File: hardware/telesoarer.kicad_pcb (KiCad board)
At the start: 2 copper layers, 37.2 x 16 mm, 30 parts, among them IC1 ATMEGA328P, K1 RC SIG IN, K2 G T R, P1 ATMEL ISP, P2 PZ, P3 PZ_IN, P4 AOUT, Q1 BC847C, Q2 2N7000, U1 MS5611

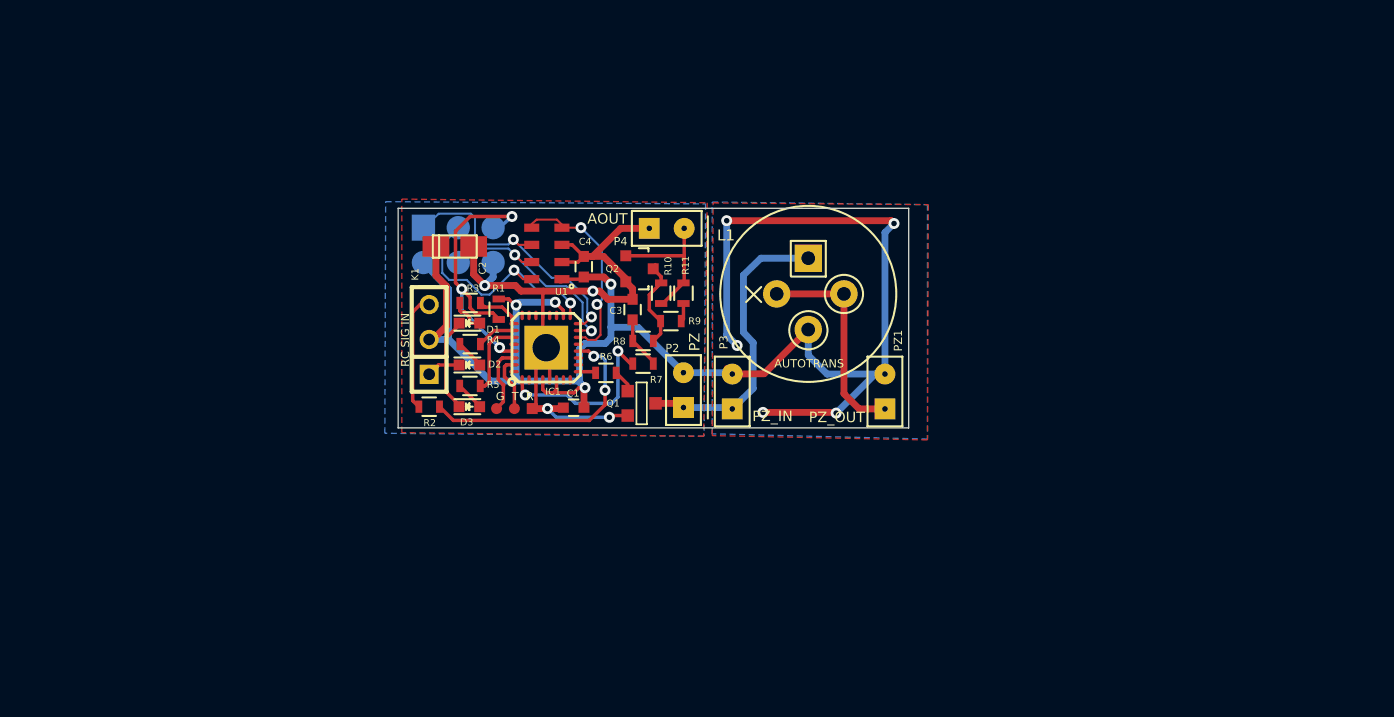
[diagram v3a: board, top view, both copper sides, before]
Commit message: Switching to NXP ARM chip. Added reference files.
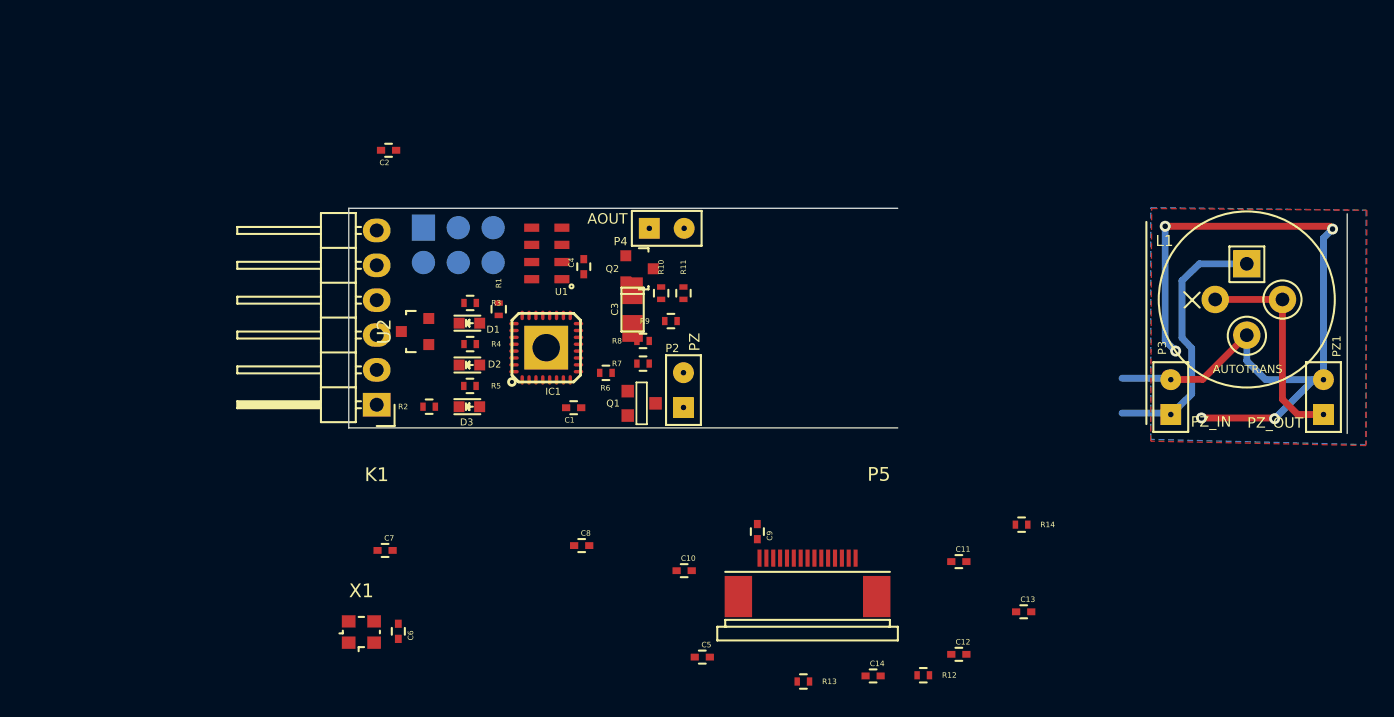
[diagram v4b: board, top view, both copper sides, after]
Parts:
- removed K2: G T R, footprints:TP-3
- added C10: 1u, footprints:C_0402, F.Cu at (64.4, 57.4)
- added C11: 1u, footprints:C_0402, F.Cu at (84.5, 56.7)
- added C12: 1u, footprints:C_0402, F.Cu at (84.5, 63.5)
- added C13: 2u2, footprints:C_0402, F.Cu at (89.2, 60.4)
- added C14: 2u2, footprints:C_0402, F.Cu at (78.2, 65.1)
- added C5: 0u1, footprints:C_0402, F.Cu at (65.8, 63.7)
- added C6: 18p, footprints:C_0402, F.Cu at (43.6, 61.8)
- added C7: 0u1, footprints:C_0402, F.Cu at (42.6, 55.9)
- added C8: 0u1, footprints:C_0402, F.Cu at (57.0, 55.6)
- added C9: 1u, footprints:C_0402, F.Cu at (69.8, 54.6)
- added P5: OLED 0.91" 128x32, footprints:ZIF_FPC15, F.Cu at (73.4, 56.5)
- added R12: 330K, footprints:R_0402, F.Cu at (81.9, 65.0)
- added R13: 1K, footprints:R_0402, F.Cu at (73.1, 65.5)
- added R14: 390K, footprints:R_0402, F.Cu at (89.0, 54.1)
- added U2: MCP1703T-3302, footprints:SOT-23A, F.Cu at (44.8, 40.0)
- added X1: 16MHz, Crystals:Crystal_SMD_2520_4Pads, F.Cu at (40.9, 61.9)
- C1: footprint footprints:C_0603 -> footprints:C_0402
- C2: value 22u -> 0u1; footprint footprints:TantalC_SizeS_EIA-3216 -> footprints:C_0402
- C3: value 0u1 -> 22u; footprint footprints:C_0603 -> footprints:TantalC_SizeS_EIA-3216
- C4: value 0u1 -> 18p; footprint footprints:C_0603 -> footprints:C_0402
- K1: value RC SIG IN -> DATA; footprint footprints:SIL-3 -> Pin_Headers:Pin_Header_Angled_1x06
- R1: value 5K6 -> 10K; footprint footprints:R_0603 -> footprints:R_0402
- R10: value 330K -> 220K; footprint footprints:R_0603 -> footprints:R_0402
- R11: value 1K -> 220K; footprint footprints:R_0603 -> footprints:R_0402
- R2: value 200 -> 1K; footprint footprints:R_0603 -> footprints:R_0402
- R3, R4, R5, R6: footprint footprints:R_0603 -> footprints:R_0402
- R7: value 56K -> 0; footprint footprints:R_0603 -> footprints:R_0402
- R8: value 220K -> 56K; footprint footprints:R_0603 -> footprints:R_0402
- R9: value 220K -> 1K; footprint footprints:R_0603 -> footprints:R_0402
- moved P3 32.0 mm to (99.9, 44.8)
- moved L1 32.0 mm to (105.4, 37.6)
- moved PZ1 32.0 mm to (111.0, 44.8)
- moved C2 8.51 mm to (42.9, 26.8)
- moved K1 6.10 mm to (42.0, 45.3), turned to 180 degrees
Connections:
- net /~SS renamed /SENS_~SS
- C1 pad 1: +5V -> +3V3
- C1 pad 2: GND -> (no net)
- C2 pad 1: +5V -> /~RESET
- C2 pad 2: GND -> Net-(C2-Pad2)
- C3 pad 1: Net-(C3-Pad1) -> +BATT
- C4 pad 1: +5V -> Net-(C4-Pad1)
- IC1 pad 10: Net-(IC1-Pad10) -> /~RES
- IC1 pad 11: Net-(IC1-Pad11) -> /D/~C
- IC1 pad 13: Net-(IC1-Pad13) -> /OLED_~SS
- IC1 pad 18: +5V -> +3V3
- IC1 pad 19: Net-(IC1-Pad19) -> (no net)
- IC1 pad 2: Net-(IC1-Pad2) -> (no net)
- IC1 pad 20: Net-(IC1-Pad20) -> (no net)
- IC1 pad 22: Net-(IC1-Pad22) -> (no net)
- IC1 pad 23: Net-(IC1-Pad23) -> (no net)
- IC1 pad 24: Net-(IC1-Pad24) -> (no net)
- IC1 pad 28: Net-(IC1-Pad28) -> (no net)
- IC1 pad 29: /RESET -> /~RESET
- IC1 pad 4: +5V -> +3V3
- IC1 pad 6: +5V -> +3V3
- IC1 pad 7: Net-(IC1-Pad7) -> Net-(C4-Pad1)
- K1 pad 2: +5V -> +BATT
- L1 pad 2: +5V -> +BATT
- P1 pad 2: +5V -> +3V3
- P1 pad 5: /RESET -> /~RESET
- P2 pad 2: +5V -> +BATT
- P3 pad 2: +5V -> +BATT
- PZ1 pad 2: +5V -> +BATT
- R1 pad 1: /RESET -> /~RESET
- R1 pad 2: +5V -> +3V3
- R10 pad 1: Net-(P4-Pad2) -> Net-(Q2-Pad3)
- R10 pad 2: Net-(Q2-Pad3) -> Net-(C8-Pad1)
- R11 pad 2: Net-(P4-Pad2) -> Net-(Q2-Pad3)
- R6 pad 1: Net-(Q1-Pad1) -> /RX
- R6 pad 2: Net-(IC1-Pad9) -> Net-(IC1-Pad30)
- R7 pad 1: Net-(C3-Pad1) -> /TX
- R7 pad 2: Net-(IC1-Pad1) -> Net-(IC1-Pad31)
- R8 pad 1: Net-(Q2-Pad3) -> Net-(C8-Pad1)
- R8 pad 2: Net-(C3-Pad1) -> Net-(IC1-Pad1)
- R9 pad 1: +3V3 -> Net-(Q1-Pad1)
- R9 pad 2: Net-(Q2-Pad3) -> Net-(IC1-Pad9)
- U1 pad 1: +5V -> +3V3
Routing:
- net +5V: track 126.1 -> 0.00 mm, vias 9 -> 0
- net GND: track 61.8 -> 0.00 mm, vias 4 -> 0
- net +BATT: track 0.00 -> 61.6 mm, vias 0 -> 5
- net /RESET: track 21.3 -> 0.00 mm, vias 3 -> 0
- net /MISO: track 20.5 -> 0.00 mm, vias 2 -> 0
- net Net-(IC1-Pad12): track 18.3 -> 0.00 mm, vias 2 -> 0
- net /SCK: track 17.8 -> 0.00 mm, vias 2 -> 0
- net /MOSI: track 16.2 -> 0.00 mm, vias 2 -> 0
- net /SENS_~SS: track 14.7 -> 0.00 mm, vias 2 -> 0
- net Net-(IC1-Pad1): track 13.0 -> 0.00 mm, vias 2 -> 0
- net Net-(P4-Pad2): track 10.6 -> 0.00 mm
- net /SIG: track 8.51 -> 0.00 mm
- net Net-(Q2-Pad3): track 6.68 -> 0.00 mm
- net /LED_GREEN: track 5.38 -> 0.00 mm
- net Net-(IC1-Pad30): track 5.12 -> 0.00 mm
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- added copper zone on B.Cu, net +BATT
- added copper zone on F.Cu, net +BATT
- removed copper zone on B.Cu, net +5V
- removed copper zone on F.Cu, net +5V
- removed copper zone on B.Cu, net GND
- removed copper zone on F.Cu, net GND
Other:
- board size 37.2 x 16 mm -> 72.8 x 16.4 mm

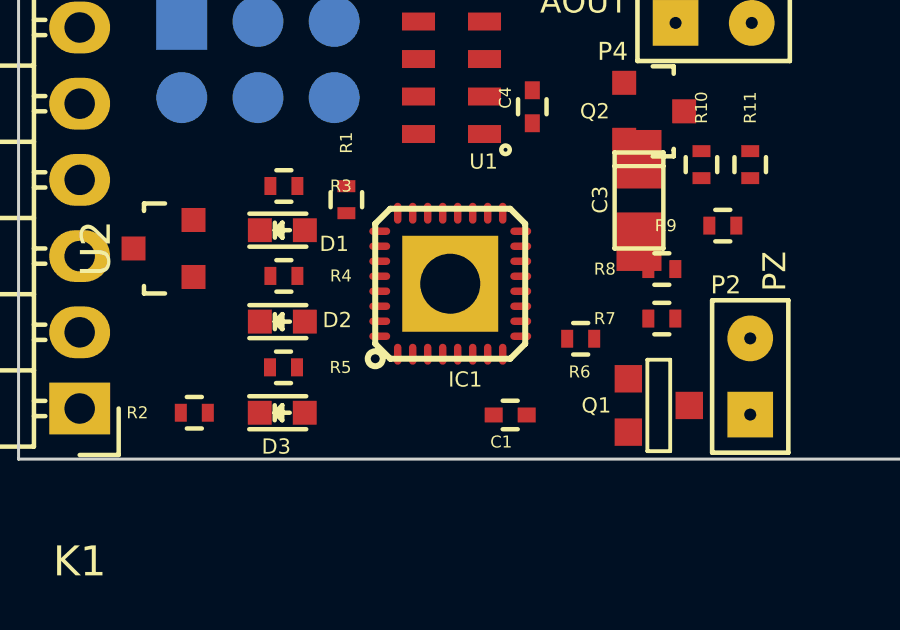
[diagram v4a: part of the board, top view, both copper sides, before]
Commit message: Ripping things apart for the change to STM32 chipa
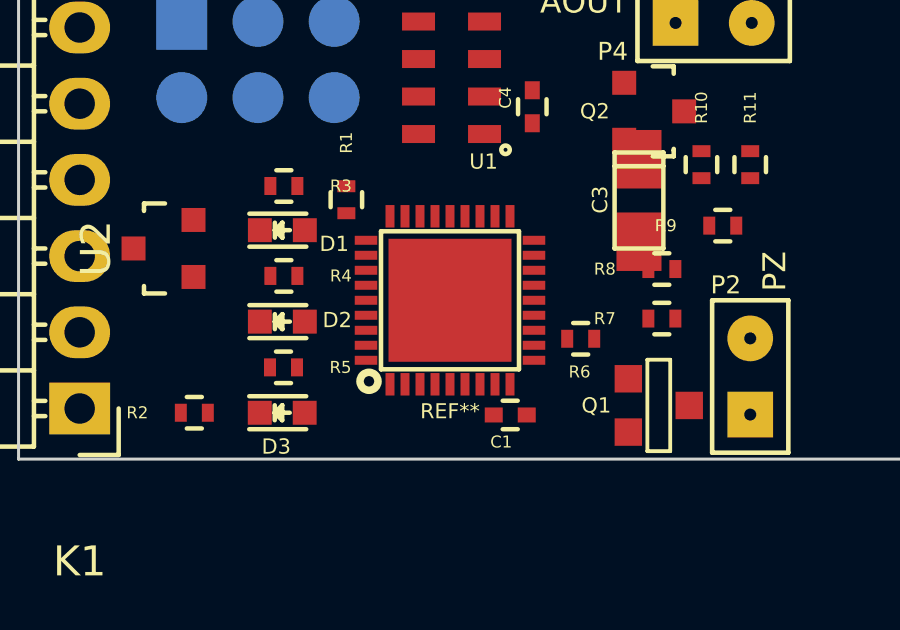
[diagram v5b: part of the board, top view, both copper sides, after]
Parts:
- removed IC1: ATMEGA328P, footprints:MLF-32_2mmVIA_SINK
- added REF**: VFQFPN36_0.5_6x6, footprints:VFQFPN36_0.5_6x6, F.Cu at (54.4, 41.7)

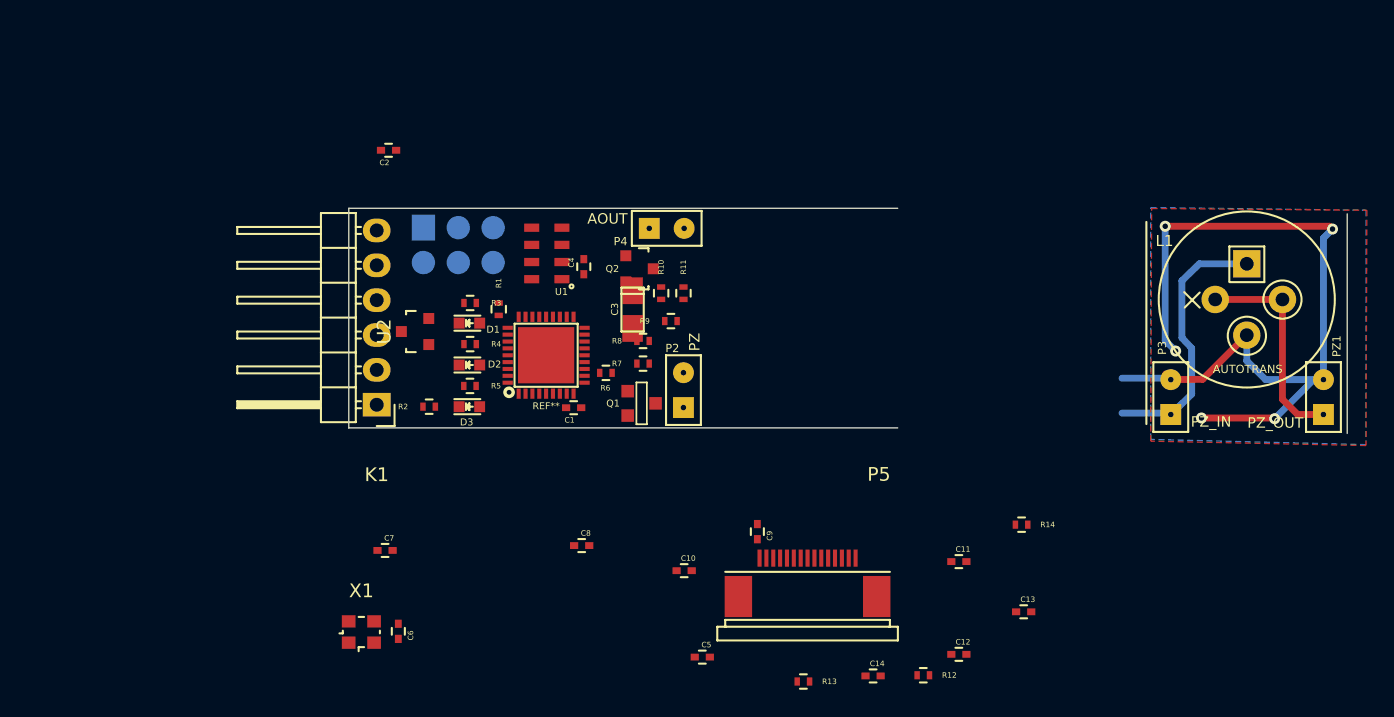
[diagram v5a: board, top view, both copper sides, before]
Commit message: Work on STM32 / OLED PCB design begins
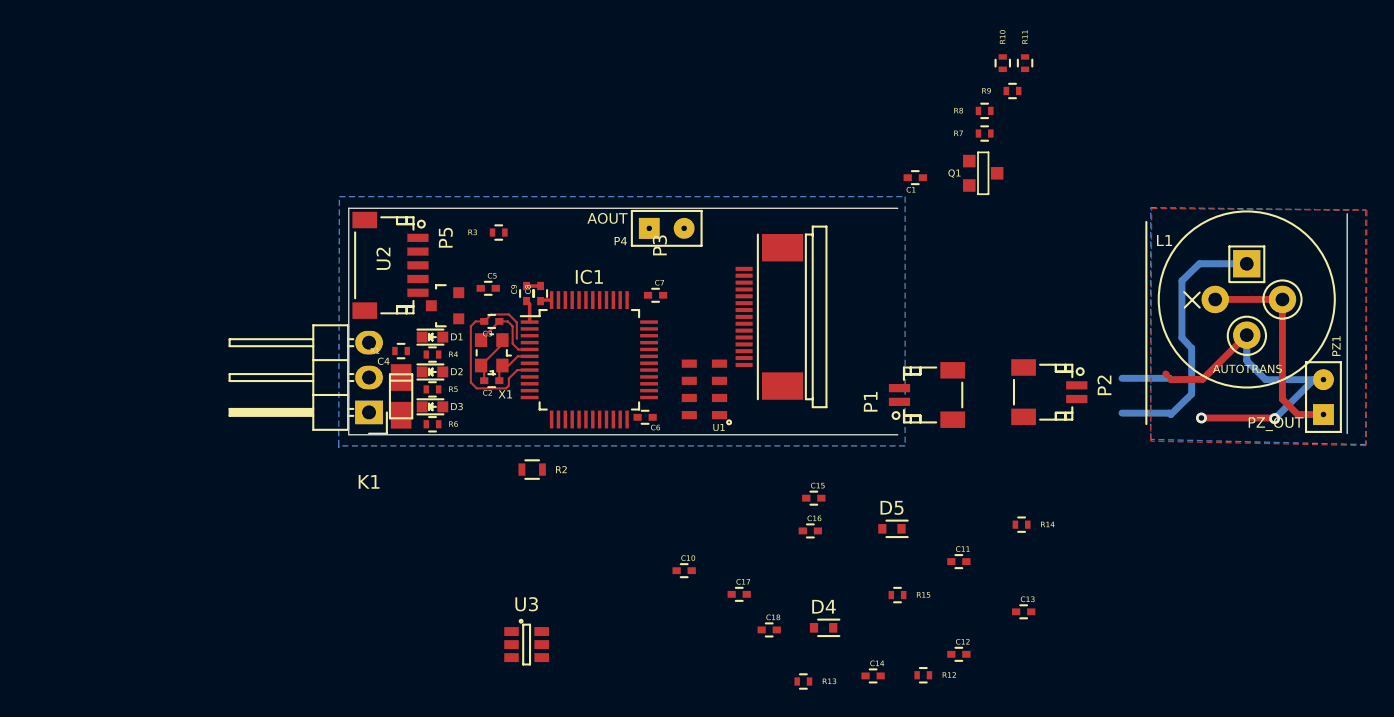
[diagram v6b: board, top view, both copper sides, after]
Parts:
- removed Q2: 2N7000, TO_SOT_Packages_SMD:SOT-23
- removed REF**: VFQFPN36_0.5_6x6, footprints:VFQFPN36_0.5_6x6
- added C15: 1u, footprints:C_0402, F.Cu at (73.9, 52.1)
- added C16: 1u, footprints:C_0402, F.Cu at (73.6, 54.5)
- added C17: 2u2, footprints:C_0402, F.Cu at (68.5, 59.1)
- added C18: 2u2, footprints:C_0402, F.Cu at (70.6, 61.7)
- added D4: D_Schottky, Diodes_SMD:SOD-523, F.Cu at (74.6, 61.6)
- added D5: D_Schottky, Diodes_SMD:SOD-523, F.Cu at (79.6, 54.4)
- added IC1: STM32F103CBT6, footprints:LQFP-48_7x7mm_Pitch0.5mm, F.Cu at (57.5, 42.0)
- added R15: 100K, footprints:R_0402, F.Cu at (80.0, 59.2)
- added U3: AD8027ARTZ, TO_SOT_Packages_SMD:SOT-23-6, F.Cu at (53.0, 62.8)
- C10, C11, C9: value 1u -> 0u1
- C13: value 2u2 -> 1u
- C14: value 2u2 -> 0u1
- C2: value 0u1 -> 18p
- C3: value 22u -> 18p; footprint footprints:TantalC_SizeS_EIA-3216 -> footprints:C_0402
- C4: value 18p -> 22u; footprint footprints:C_0402 -> footprints:TantalC_SizeS_EIA-3216
- C6: value 18p -> 0u1
- K1: value DATA -> RC_SIG; footprint Pin_Headers:Pin_Header_Angled_1x06 -> Pin_Headers:Pin_Header_Angled_1x03
- P1: value ATMEL ISP -> PZ; footprint POGO_ISP_3x2 -> Connectors_JST:JST_SH_SM02B-SRSS-TB_02x1.00mm_Angled; moved to F.Cu
- P2: value PZ -> PZ_IN; footprint footprints:PIN_ARRAY_2X1 -> Connectors_JST:JST_SH_SM02B-SRSS-TB_02x1.00mm_Angled
- P3: value PZ_IN -> OLED 0.91" 128x32; footprint footprints:PIN_ARRAY_2X1 -> footprints:ZIF_FPC15
- P5: value OLED 0.91" 128x32 -> CONN_01X05; footprint footprints:ZIF_FPC15 -> Connectors_JST:JST_SH_SM05B-SRSS-TB_05x1.00mm_Angled
- R1: value 10K -> 1K
- R10, R11: value 220K -> 5K
- R12: value 330K -> 100K
- R13: value 1K -> 100
- R2: value 1K -> NC; footprint footprints:R_0402 -> footprints:R_0603
- R3: value 1K -> 5K
- R4: value 3K9 -> 1K
- R5: value 1K5 -> 3K9
- R6: value 1K -> 1K5
- R7: value 0 -> NC
- R8: value 56K -> 5K
- moved P5 37.1 mm to (43.1, 35.2), turned to 270 degrees
- moved P1 35.8 mm to (82.1, 44.6), turned to 90 degrees
- moved P3 31.6 mm to (68.8, 38.9)
- moved C5 31.1 mm to (50.2, 36.8)
- moved R11 30.0 mm to (89.3, 20.4)
- moved Q1 30.0 mm to (86.2, 28.4)
- moved C1 30.0 mm to (81.3, 28.8)
- moved R10 30.0 mm to (87.7, 20.4)
- moved R9 30.0 mm to (88.4, 22.5)
- moved R7 30.0 mm to (86.3, 25.6)
- moved R8 30.0 mm to (86.3, 23.9)
- moved C7 27.1 mm to (62.4, 37.3)
- moved P2 26.7 mm to (91.1, 44.4), turned to 270 degrees
- moved C9 24.2 mm to (53.0, 37.2), turned to 90 degrees
- moved C6 23.8 mm to (61.6, 46.2), turned to 0 degrees
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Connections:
- net /SENS_~SS renamed /VARIO_~SS
- C1 pad 2: (no net) -> GND
- C10 pad 1: Net-(C10-Pad1) -> +3V3
- C10 pad 2: Net-(C10-Pad2) -> GND
- C11 pad 1: GND -> Net-(C11-Pad1)
- C11 pad 2: +3V3 -> GND
- C12 pad 1: +3V3 -> Net-(C12-Pad1)
- C12 pad 2: GND -> Net-(C12-Pad2)
- C13 pad 2: GND -> Net-(C13-Pad2)
- C2 pad 1: /~RESET -> Net-(C2-Pad1)
- C2 pad 2: Net-(C2-Pad2) -> GND
- C3 pad 1: +BATT -> Net-(C3-Pad1)
- C4 pad 1: Net-(C4-Pad1) -> +BATT
- C6 pad 1: Net-(C6-Pad1) -> +3V3
- C8 pad 1: Net-(C8-Pad1) -> +3V3
- C9 pad 1: Net-(C9-Pad1) -> +3V3
- C9 pad 2: Net-(C9-Pad2) -> GND
- P1 pad 1: /MISO -> Net-(L1-Pad1)
- P1 pad 2: +3V3 -> +BATT
- P3 pad 1: Net-(L1-Pad1) -> Net-(C12-Pad2)
- P3 pad 2: +BATT -> Net-(C12-Pad1)
- P5 pad 1: Net-(C9-Pad2) -> GND
- P5 pad 2: Net-(C9-Pad1) -> /SWDCLK
- P5 pad 3: Net-(C10-Pad2) -> /SWDIO
- P5 pad 4: Net-(C10-Pad1) -> /USART1_TX
- P5 pad 5: +3V3 -> /USART1_RX
- R1 pad 1: /~RESET -> Net-(IC1-Pad43)
- R1 pad 2: +3V3 -> /SIG
- R10 pad 1: Net-(Q2-Pad3) -> Net-(C11-Pad1)
- R10 pad 2: Net-(C8-Pad1) -> /VARIO_OUT
- R11 pad 1: +3V3 -> Net-(C14-Pad1)
- R11 pad 2: Net-(Q2-Pad3) -> Net-(C11-Pad1)
- R12 pad 1: Net-(P4-Pad2) -> Net-(C14-Pad1)
- R12 pad 2: Net-(Q2-Pad3) -> Net-(R12-Pad2)
- R13 pad 1: +3V3 -> GND
- R13 pad 2: Net-(P4-Pad2) -> Net-(R13-Pad2)
- R14 pad 1: Net-(P5-Pad13) -> Net-(P3-Pad13)
- R2 pad 1: Net-(IC1-Pad12) -> Net-(IC1-Pad44)
- R2 pad 2: /SIG -> +3V3
- R3 pad 1: Net-(D1-Pad2) -> Net-(IC1-Pad44)
- R3 pad 2: /LED_RED -> GND
- R4 pad 1: Net-(D2-Pad2) -> Net-(D1-Pad2)
- R4 pad 2: /LED_BLUE -> /LED_RED
- R5 pad 1: Net-(D3-Pad2) -> Net-(D2-Pad2)
- R5 pad 2: /LED_GREEN -> /LED_BLUE
- R6 pad 1: /RX -> Net-(D3-Pad2)
- R6 pad 2: Net-(IC1-Pad30) -> /LED_GREEN
- R7 pad 1: /TX -> GND
- R7 pad 2: Net-(IC1-Pad31) -> /~RESET
- R8 pad 1: Net-(C8-Pad1) -> +3V3
- R8 pad 2: Net-(IC1-Pad1) -> /~RESET
- X1 pad 1: Net-(C4-Pad1) -> Net-(C2-Pad1)
- X1 pad 2: Net-(C6-Pad1) -> Net-(C3-Pad1)
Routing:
- net +BATT: track 61.6 -> 25.0 mm, vias 5 -> 2
- net GND: track 0.00 -> 19.9 mm
- net Net-(C3-Pad1): track 0.00 -> 5.99 mm
- net (no net): track 0.00 -> 3.69 mm
- net Net-(C2-Pad1): track 0.00 -> 3.46 mm
- net +3V3: track 0.00 -> 2.45 mm
- added copper zone on B.Cu, net GND
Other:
- board size 72.8 x 16.4 mm -> 72.8 x 16.5 mm
- net class +5V: clearance 0.15 -> 0.1524; trace_width 0.5 -> 0.508; via_dia 0.8 -> 0.8636; via_drill 0.4 -> 0.4572
- net class Default: clearance 0.15 -> 0.1524; trace_width 0.254 -> 0.1524; via_dia 0.8 -> 0.6858; via_drill 0.4 -> 0.3302
- net class GND: clearance 0.15 -> 0.1524; trace_width 0.5 -> 0.508; via_dia 0.8 -> 0.8636; via_drill 0.4 -> 0.4572
- rule trace_clearance: 0.15 -> 0.1524
- rule trace_min: 0.15 -> 0.1524
- rule via_min_drill: 0.4 -> 0.3302
- rule via_min_size: 0.65 -> 0.6858
